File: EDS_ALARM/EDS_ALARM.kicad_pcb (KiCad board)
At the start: 2 copper layers, 58.4 x 41.9 mm, 28 parts, among them J1 USB_B_Micro, J2 Conn_01x06_Male, J3 73412-0110, SW1 SW_Push, U1 EKMC1601111, U2 CMWX1ZZABZ-078, U3 LT1117-3.3, U4 TGS2611-E00

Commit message: s
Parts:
- added D3: LED, LED_SMD:LED_0805_2012Metric, F.Cu at (246.1, 118.3)
- added J4: Conn_01x02_Male, Connector_PinSocket_2.54mm:PinSocket_1x02_P2.54mm_Vertical, F.Cu at (241.6, 116.1)
- added R2: 680, Resistor_SMD:R_0805_2012Metric_Pad1.15x1.40mm_HandSolder, F.Cu at (230.5, 123.1)
- added R3: ??, Resistor_SMD:R_0805_2012Metric_Pad1.15x1.40mm_HandSolder, F.Cu at (241.6, 122.4)
- added R4: 10k, Resistor_SMD:R_0805_2012Metric_Pad1.15x1.40mm_HandSolder, F.Cu at (235.2, 123.1)
- added R5: ??, Resistor_SMD:R_0805_2012Metric_Pad1.15x1.40mm_HandSolder, F.Cu at (246.2, 115.3)
- added SW2: SW_Push, Button_Switch_SMD:SW_SPST_PTS645, F.Cu at (233.7, 117.7)
- J2: value Conn_01x06_Male -> Conn_01x05_Male; footprint Connector_PinHeader_2.54mm:PinHeader_1x06_P2.54mm_Vertical -> Connector_PinSocket_2.54mm:PinSocket_1x05_P2.54mm_Vertical
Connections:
- D1 pad 2: +3V3 -> Net-(D1-Pad2)
- D2 pad 2: /LED2 -> Net-(D2-Pad2)
- J1 pad 2: Net-(J1-Pad2) -> (no net)
- J1 pad 3: Net-(J1-Pad3) -> (no net)
- J1 pad 4: Net-(J1-Pad4) -> (no net)
- U2 pad 1: Net-(U2-Pad1) -> (no net)
- U2 pad 10: Net-(U2-Pad10) -> (no net)
- U2 pad 11: Net-(U2-Pad11) -> (no net)
- U2 pad 12: Net-(U2-Pad12) -> (no net)
- U2 pad 13: Net-(U2-Pad13) -> (no net)
- U2 pad 14: Net-(U2-Pad14) -> (no net)
- U2 pad 15: Net-(U2-Pad15) -> (no net)
- U2 pad 16: Net-(U2-Pad16) -> (no net)
- U2 pad 17: Net-(U2-Pad17) -> (no net)
- U2 pad 18: Net-(U2-Pad18) -> /RX
- U2 pad 19: Net-(U2-Pad19) -> /TX
- U2 pad 2: Net-(U2-Pad2) -> (no net)
- U2 pad 28: Net-(U2-Pad28) -> (no net)
- U2 pad 29: Net-(U2-Pad29) -> (no net)
- U2 pad 30: Net-(U2-Pad30) -> (no net)
- U2 pad 31: Net-(U2-Pad31) -> (no net)
- U2 pad 33: Net-(U2-Pad33) -> (no net)
- U2 pad 35: Net-(U2-Pad35) -> (no net)
- U2 pad 36: Net-(U2-Pad36) -> (no net)
- U2 pad 37: Net-(U2-Pad37) -> (no net)
- U2 pad 38: Net-(U2-Pad38) -> (no net)
- U2 pad 39: Net-(U2-Pad39) -> (no net)
- U2 pad 40: Net-(U2-Pad40) -> (no net)
- U2 pad 46: Net-(U2-Pad46) -> Net-(U2-Pad45)
- U2 pad 47: Net-(U2-Pad47) -> +3V3
- U2 pad 8: Net-(U2-Pad8) -> (no net)
- U2 pad 9: Net-(U2-Pad9) -> (no net)
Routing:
- net +3V3: track 128.6 -> 122.2 mm
- net /LED2: track 3.86 -> 2.59 mm

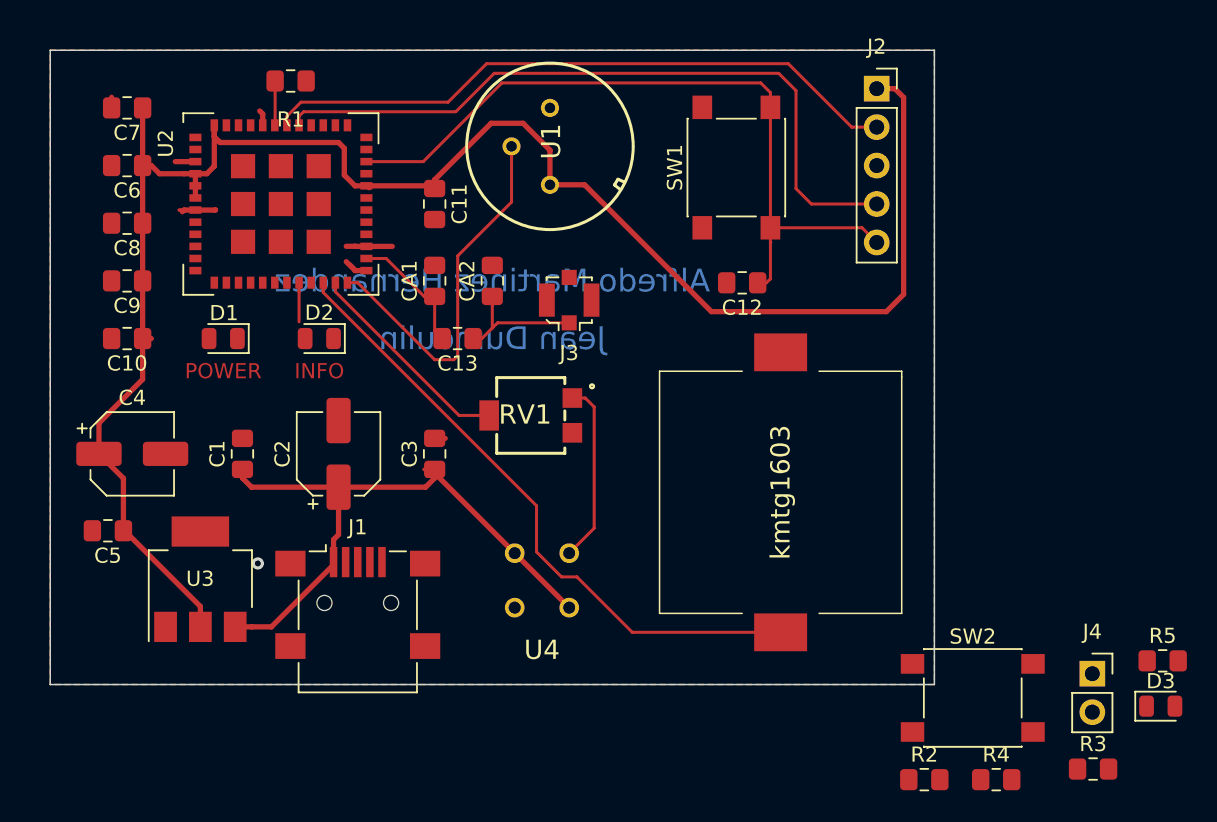
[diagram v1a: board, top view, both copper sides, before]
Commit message: Adding button, buzzer's LED
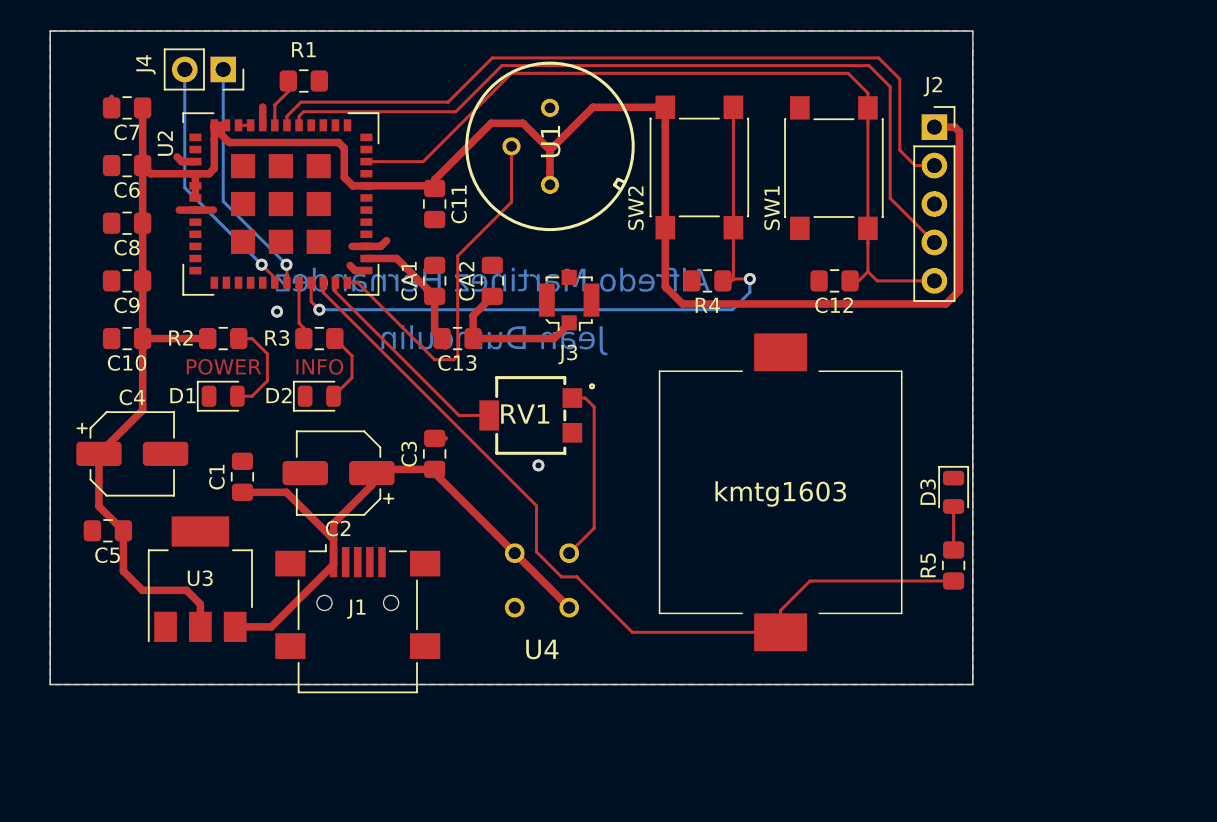
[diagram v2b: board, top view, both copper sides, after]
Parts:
- moved J4 69.9 mm to (184.2, 76.2), turned to 270 degrees
- moved R3 58.5 mm to (190.5, 94.0), turned to 180 degrees
- moved R2 54.7 mm to (184.2, 94.0), turned to 180 degrees
- moved SW2 39.4 mm to (215.6, 82.7), turned to 90 degrees
- moved R4 38.1 mm to (216.1, 90.2), turned to 180 degrees
- moved D3 19.7 mm to (232.4, 104.1), turned to 270 degrees
- moved R5 15.2 mm to (232.4, 109.0), turned to 270 degrees
- moved SW1 6.45 mm to (224.5, 82.7)
- moved C12 6.11 mm to (224.5, 90.2)
- moved J2 4.58 mm to (231.1, 80.0)
- moved D1 3.81 mm to (184.2, 97.8), turned to 0 degrees
- moved D2 3.81 mm to (190.5, 97.8), turned to 0 degrees
- moved C1 1.52 mm to (185.4, 103.1)
- moved C2 1.27 mm to (191.8, 102.9), turned to 180 degrees
- moved R1 0.87 mm to (189.5, 77.0)
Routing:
- net Net-(R4-Pad1): track 0.00 -> 45.0 mm, vias 0 -> 2
- net +3V3: track 122.2 -> 156.6 mm
- net /RX: track 0.00 -> 16.6 mm, vias 0 -> 1
- net /NRST: track 69.8 -> 54.0 mm
- net /TX: track 0.00 -> 15.8 mm, vias 0 -> 1
- net /DAC1: track 42.6 -> 56.2 mm
- net /SWDIO: track 66.1 -> 53.1 mm
- net /SWCLK: track 42.7 -> 50.7 mm
- net GND: track 17.4 -> 9.85 mm, vias 1 -> 2
- net Net-(D1-Pad2): track 0.00 -> 6.50 mm
- net Net-(D2-Pad2): track 0.00 -> 4.79 mm
- net Net-(D3-Pad2): track 0.00 -> 2.87 mm
- net Net-(C13-Pad1): track 8.87 -> 10.1 mm
- net /LED2: track 2.59 -> 3.82 mm
- net Net-(U2-Pad45): track 0.00 -> 0.80 mm
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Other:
- board size 58.4 x 41.9 mm -> 61 x 43.2 mm
- net class Antenna added: clearance 0.2, trace_width 0.5, via_dia 0.8, via_drill 0.4
- net class Power: trace_width 0.35 -> 0.5

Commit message: s
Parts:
- U2: footprint RF_Module:CMWX1ZZABZ -> RF_Module:CMWX1ZZABZ_NEW
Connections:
- U2 pad 1: (no net) -> Net-(U2-Pad1)
- U2 pad 10: (no net) -> Net-(U2-Pad10)
- U2 pad 11: (no net) -> Net-(U2-Pad11)
- U2 pad 12: (no net) -> Net-(U2-Pad12)
- U2 pad 13: (no net) -> Net-(U2-Pad13)
- U2 pad 14: (no net) -> Net-(U2-Pad14)
- U2 pad 15: (no net) -> Net-(U2-Pad15)
- U2 pad 16: (no net) -> Net-(U2-Pad16)
- U2 pad 17: (no net) -> Net-(U2-Pad17)
- U2 pad 2: (no net) -> Net-(U2-Pad2)
- U2 pad 28: (no net) -> Net-(U2-Pad28)
- U2 pad 29: (no net) -> Net-(U2-Pad29)
- U2 pad 30: (no net) -> Net-(U2-Pad30)
- U2 pad 31: (no net) -> Net-(U2-Pad31)
- U2 pad 33: (no net) -> Net-(U2-Pad33)
- U2 pad 35: (no net) -> Net-(U2-Pad35)
- U2 pad 36: (no net) -> Net-(U2-Pad36)
- U2 pad 37: (no net) -> Net-(U2-Pad37)
- U2 pad 38: (no net) -> Net-(U2-Pad38)
- U2 pad 39: (no net) -> Net-(U2-Pad39)
- U2 pad 40: (no net) -> Net-(U2-Pad40)
- U2 pad 8: (no net) -> Net-(U2-Pad8)
- U2 pad 9: (no net) -> Net-(U2-Pad9)
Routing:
- net /SWCLK: track 50.7 -> 39.6 mm
- net /SWDIO: track 53.1 -> 43.1 mm
- net Net-(R4-Pad1): vias 2 -> 1
- net GND: vias 2 -> 1
- net /RX: vias 1 -> 2

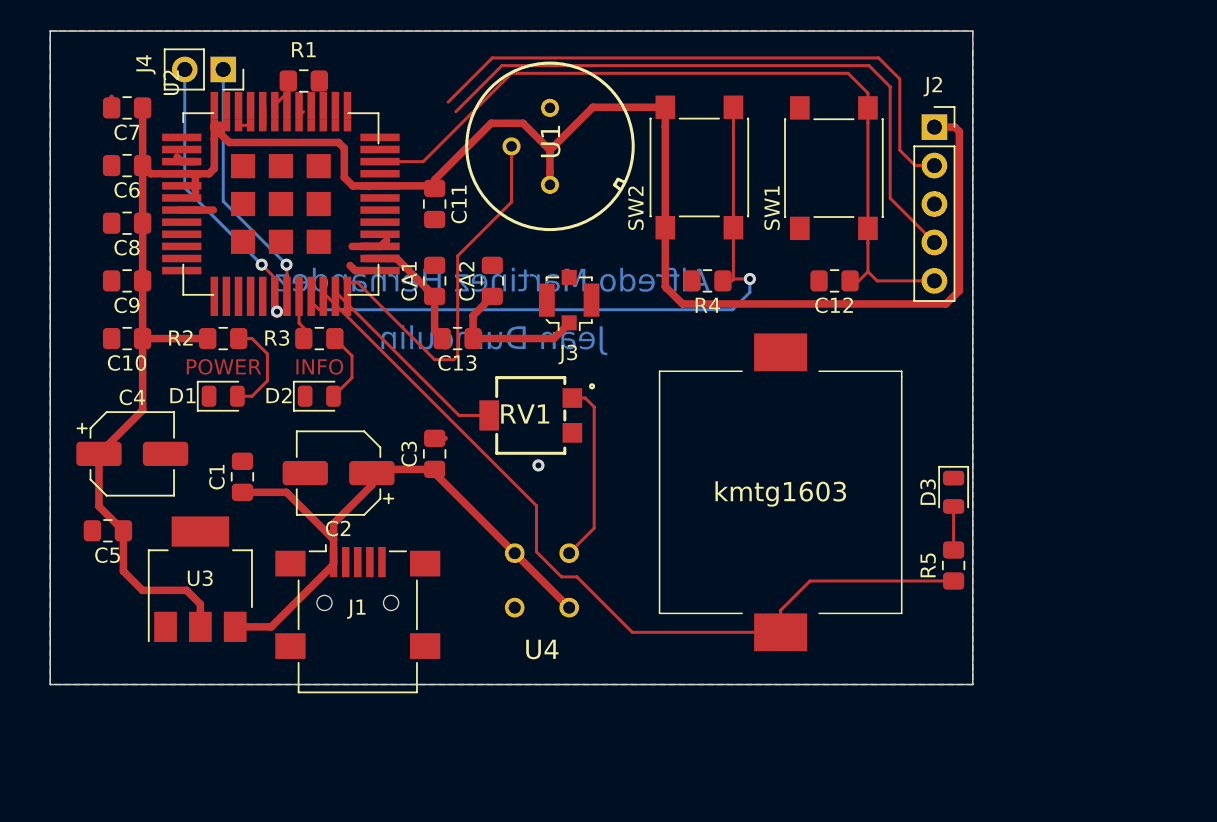
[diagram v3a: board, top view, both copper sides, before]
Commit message: MCU footprint updating
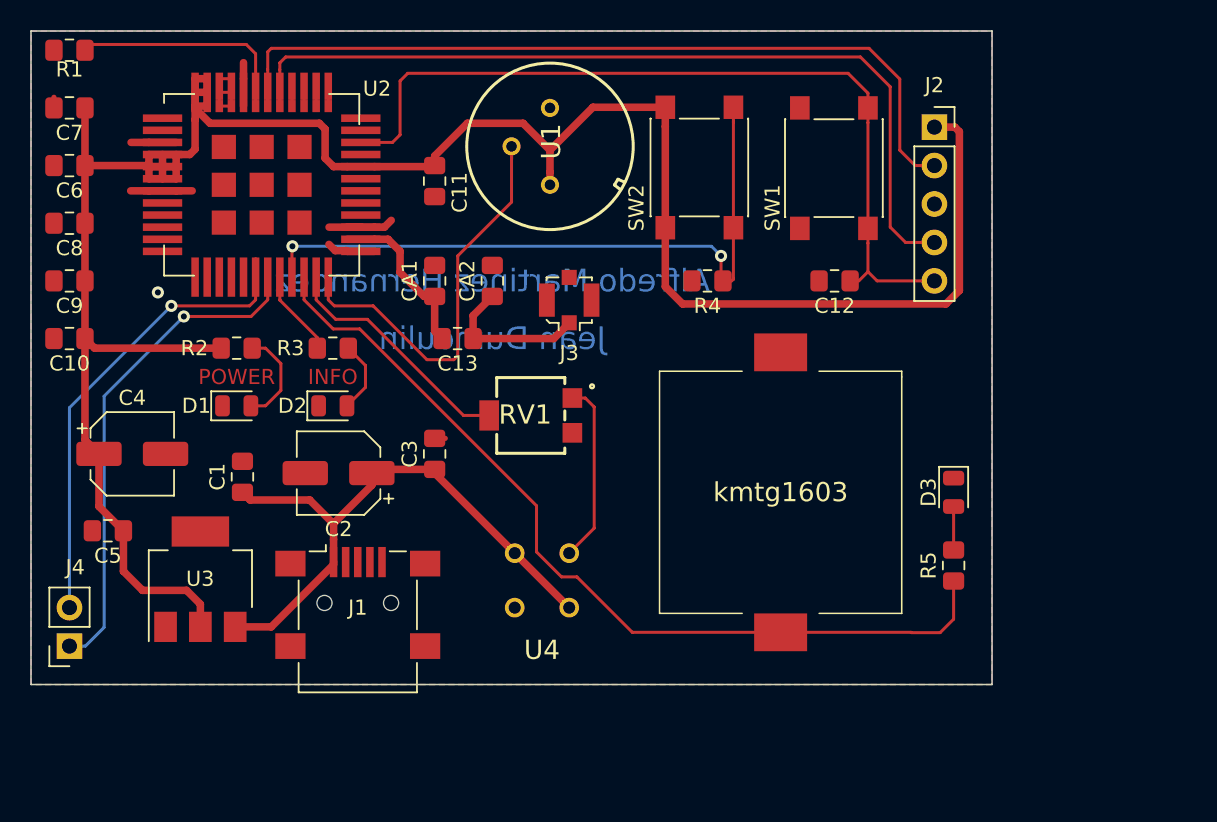
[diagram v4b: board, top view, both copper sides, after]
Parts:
- moved J4 39.4 mm to (174.0, 114.3), turned to 180 degrees
- moved R1 15.6 mm to (174.0, 74.9), turned to 180 degrees
- moved C10 3.81 mm to (174.0, 94.0)
- moved C6 3.81 mm to (174.0, 82.5)
- moved C7 3.81 mm to (174.0, 78.7)
- moved C8 3.81 mm to (174.0, 86.4)
- moved C9 3.81 mm to (174.0, 90.2)
- moved U2 1.80 mm to (186.7, 83.8)
- moved C11 1.52 mm to (198.1, 83.6)
- moved D2 1.09 mm to (191.4, 98.4)
- moved R3 1.09 mm to (191.4, 94.6)
- moved D1 1.09 mm to (185.0, 98.4)
- moved R2 1.09 mm to (185.0, 94.6)
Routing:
- net /TX: track 15.8 -> 33.9 mm
- net /SWCLK: track 39.6 -> 54.3 mm
- net /RX: track 16.6 -> 31.2 mm, vias 2 -> 1
- net /SWDIO: track 43.1 -> 57.4 mm
- net Net-(R1-Pad1): track 3.32 -> 15.3 mm
- net GND: track 9.85 -> 19.8 mm
- net Net-(U2-Pad45): track 0.80 -> 6.02 mm
- net /ADC2: track 25.7 -> 28.9 mm
- net /DAC1: track 56.2 -> 59.1 mm
- net /ADC3: track 14.1 -> 17.0 mm
- net /NRST: track 54.0 -> 56.8 mm
- net Net-(C13-Pad2): track 8.54 -> 11.1 mm
- net /LED2: track 3.82 -> 6.32 mm
- net Net-(U2-Pad40): track 0.00 -> 1.81 mm
- net Net-(U2-Pad39): track 0.00 -> 1.81 mm
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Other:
- board size 61 x 43.2 mm -> 63.5 x 43.2 mm

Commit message: s
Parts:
- J1: footprint Connector_USB:USB_Mini-B_Lumberg_2486_01_Horizontal -> Connector_USB:USB_Micro-B_Wuerth_629105150521
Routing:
- net GND: track 19.8 -> 22.2 mm
- net +5V: track 40.4 -> 42.3 mm
